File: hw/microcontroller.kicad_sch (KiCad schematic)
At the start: 71 parts, among them J201 68710814022, J202 FTSH-105-01-L-DV-K, SW201 Push button switch, U201 STM32H743VIT6, U202 USB3343, Y201 26MHz, Y202 26MHz

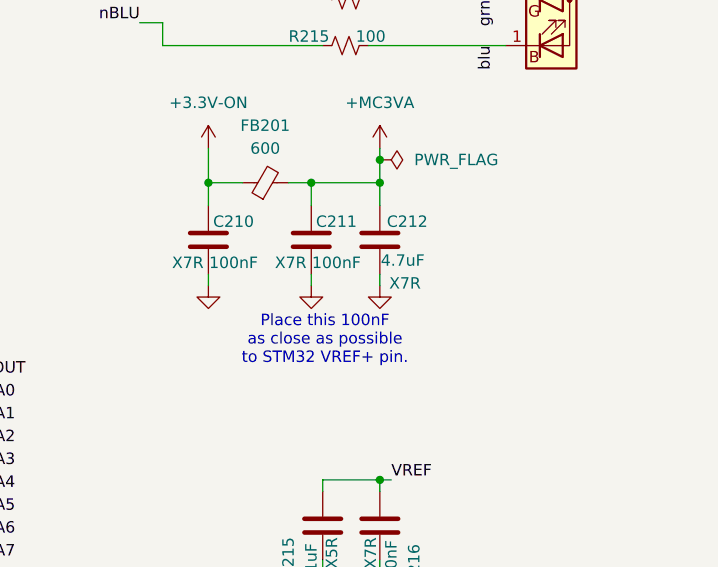
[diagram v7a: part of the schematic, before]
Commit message: Switch to parts I can source from Mouser
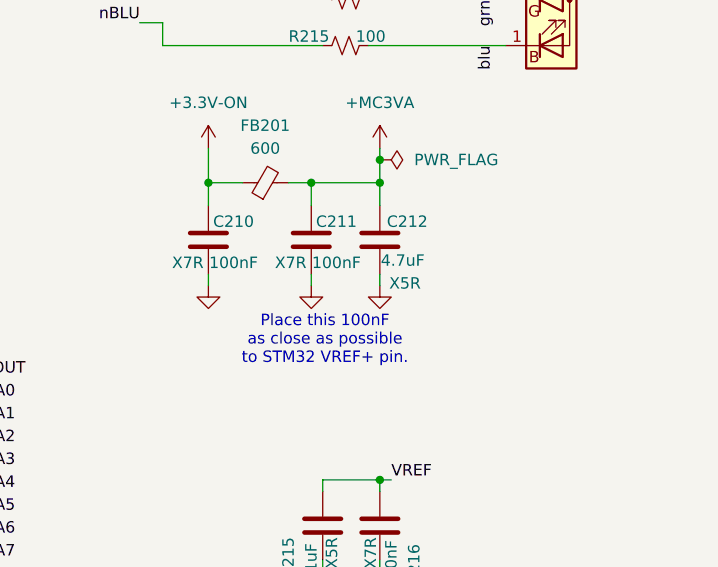
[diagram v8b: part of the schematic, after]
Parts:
- C201, C202, C203, C221, C222, C223, C224, C225: MFG (none) -> Samsung; MPN (none) -> CL05A106MP6NUN8; Mouser Part Number (none) -> 187-CL05A106MP6NUN8
- C204, C205, C217, C218: MFG (none) -> Kyocera; MPN (none) -> 04023A270JAT2A; Mouser Part Number (none) -> 581-04023A270JAT2A
- C206, C209, C213, C214, C215, C226: MFG (none) -> muRata; MPN (none) -> GRM155R61E105MA12D; Mouser Part Number (none) -> 81-GRM155R61E105MA2D
- C207, C208, C210, C211, C216, C227, C228, C229, C230, C231, C232, C233: MFG (none) -> muRata; MPN (none) -> GCM155R71H104KE02D; Mouser Part Number (none) -> 81-GCM155R71H104KE2D
- C212: MFG (none) -> Kyocera; MPN (none) -> CM05X5R475M10AH; Mouser Part Number (none) -> 346-CM05X5R475M10AH; cap-type X7R -> X5R; working-voltage 25V -> 10V
- C219, C220: MFG (none) -> TAIYO YUDEN; MPN (none) -> TMK105CBJ225MV-F; Mouser Part Number (none) -> 963-TMK105CBJ225MV-F
- D201: Mouser Part Number (none) -> 941-UHD1AA3K3E3V53Z3
- FB201: MFG (none) -> Laird; Mouser Part Number (none) -> 875-MI0603J601R-10
- J201: MFG (none) -> molex; MPN 5034800800 -> 503480-0800; Mouser Part Number (none) -> 538-503480-0800
- J202: MFG (none) -> Samtec; MPN (none) -> FTSH-105-01-L-DV-K; Mouser Part Number (none) -> 200-FTSH10501LDVK
